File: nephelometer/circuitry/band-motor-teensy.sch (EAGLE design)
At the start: 20 parts, among them IC3 7805TV, J1 2.1MMJACKTHM, U1 MotA, U2 MotA

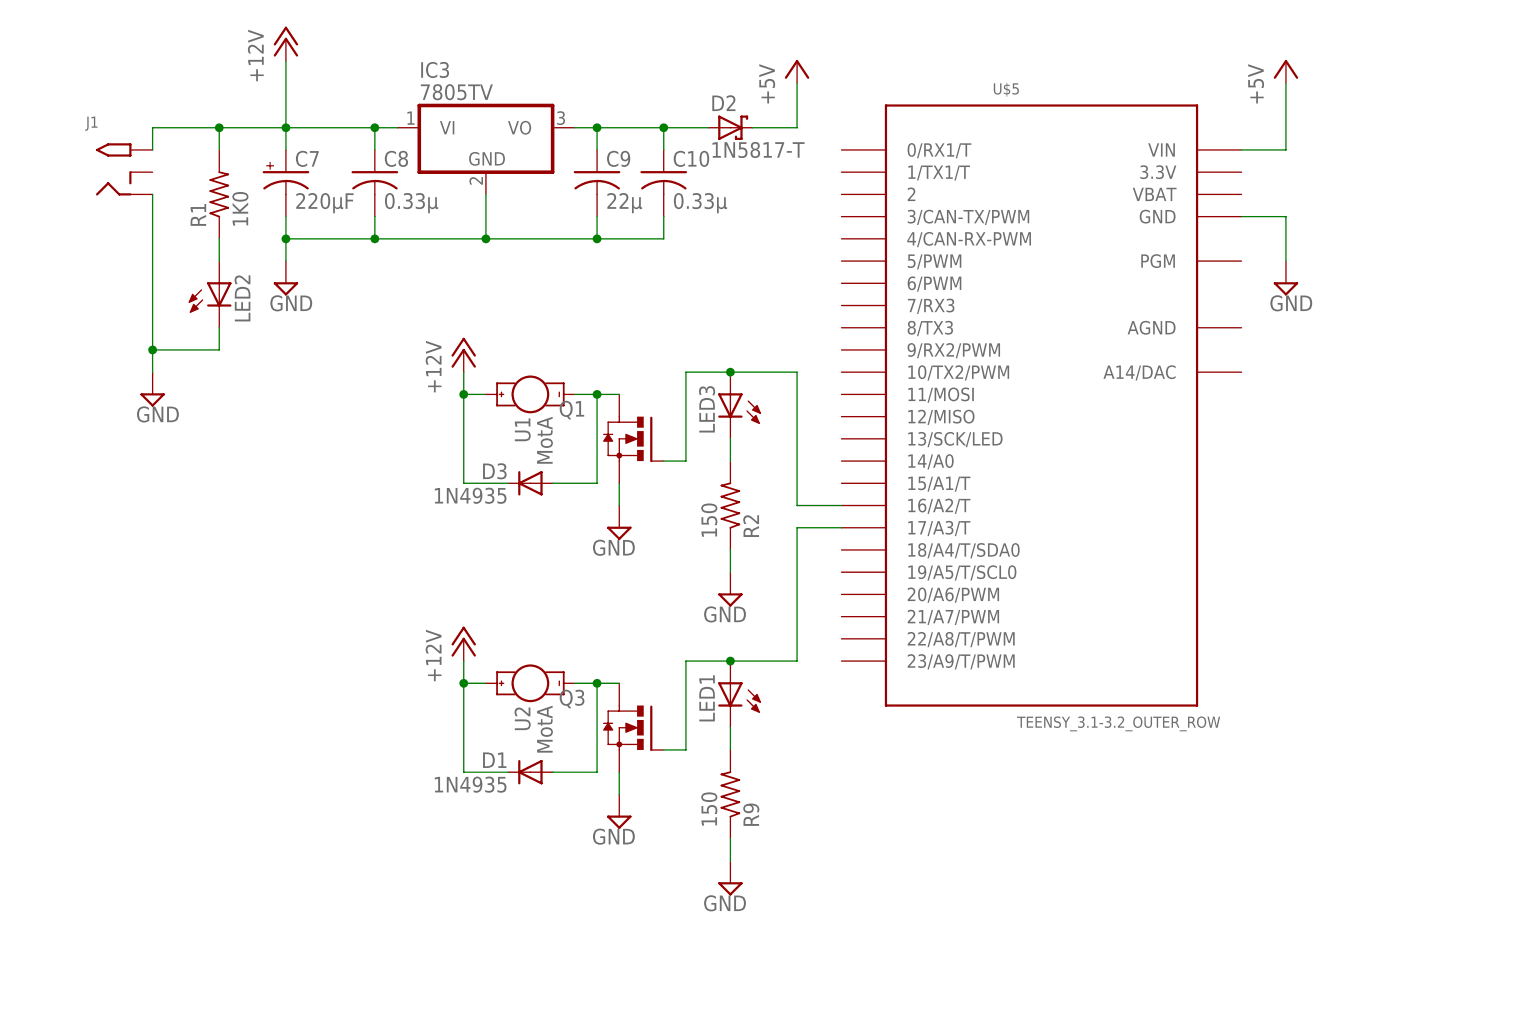
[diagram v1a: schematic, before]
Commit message: Designed motor power board to stack on nephelometer or run over RJ11 cable
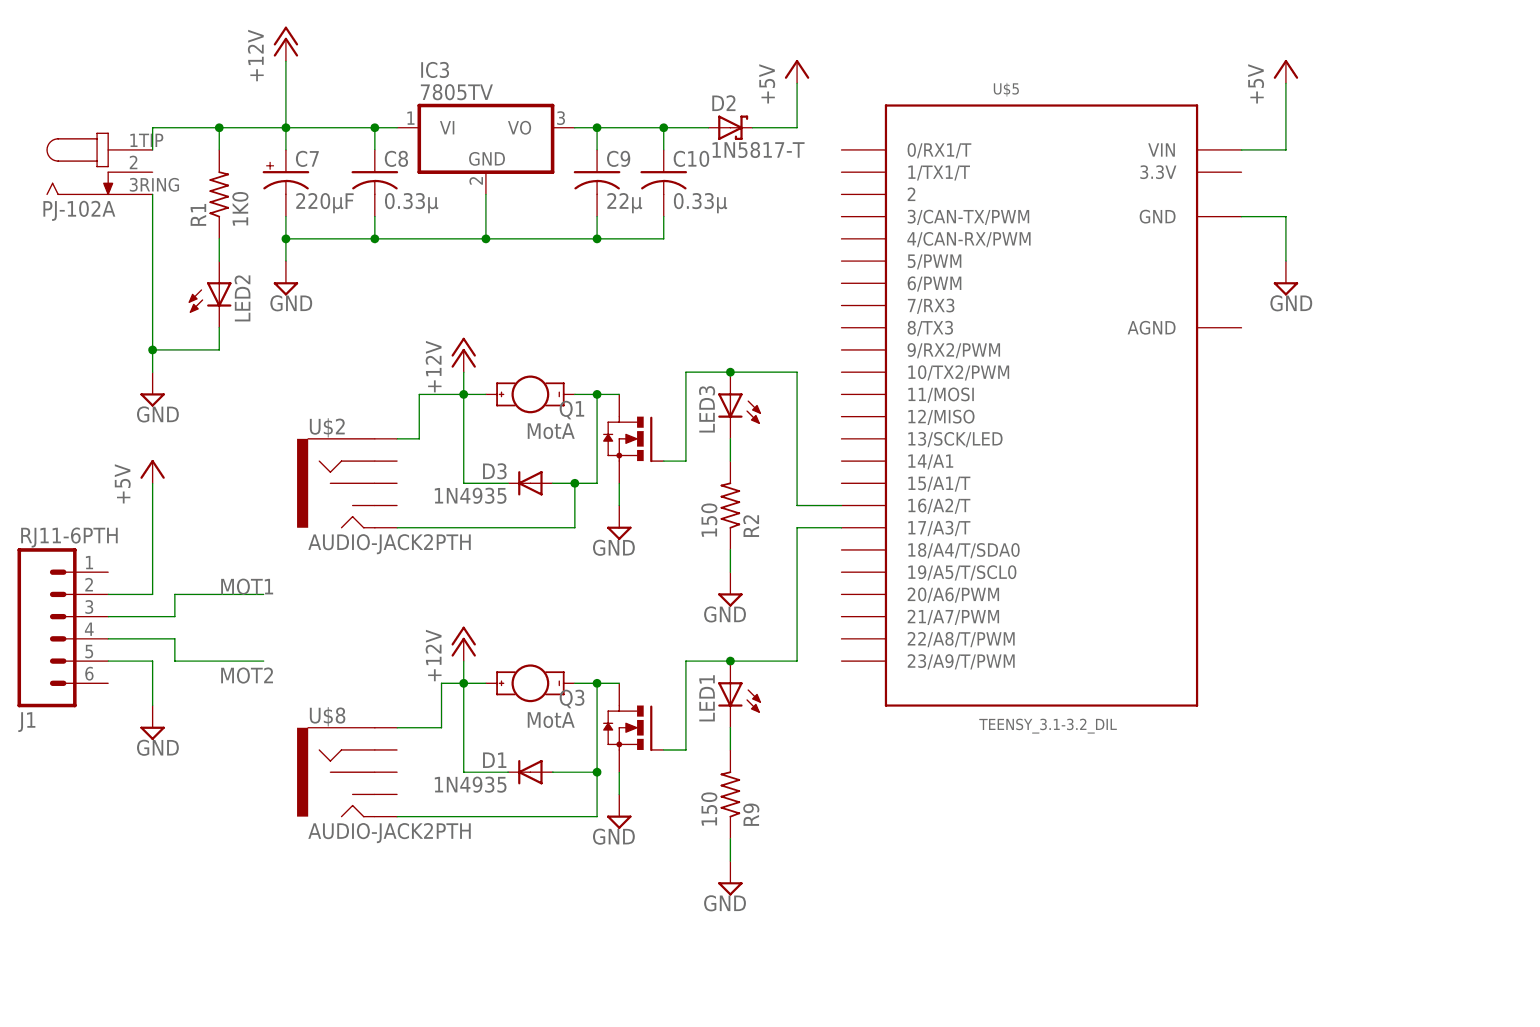
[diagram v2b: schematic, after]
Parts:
- added U$1: PJ-102A, ingolia:PJ-102A
- added U$2, U$8: AUDIO-JACK2PTH, SparkFun-Connectors:AUDIO-JACK2PTH
- J1: value 2.1MMJACKTHM -> RJ11-6PTH; device adafruit:2.1MMJACKTHM -> SparkFun-Connectors:RJ11-6PTH; DIGIKEY# CP-102A-ND -> (none); DIGIKEY2# 102-3623-ND -> (none); MANF CUI Inc -> (none); MANF# PJ-102A -> (none); MANF2 CUI Inc -> (none); MANF2# SWI24-12-N-P5 -> (none)
- R2, R9: device adafruit:R-US_0204/2V -> adafruit:R-US_0207/10
- U$5: value TEENSY_3.1-3.2_OUTER_ROW -> TEENSY_3.1-3.2_DIL; device Teensy_3_and_LC_Series_Boards_v1.4:TEENSY_3.1-3.2_OUTER_ROW -> Teensy_3_and_LC_Series_Boards_v1.4:TEENSY_3.1-3.2_DIL
- U1, U2: device ingolia:1X02_MOTOR -> ingolia:1X02_3.5MM_MOT
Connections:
- removed net N$19: LED1.A, Q3.G, U$5.17/A3/T
- removed net N$6: LED3.A, Q1.G, U$5.16/A2/T
- new net MOT1: J1.3, LED3.A, Q1.G, U$5.16/A2/T
- new net MOT2: J1.4, LED1.A, Q3.G, U$5.17/A3/T
- net +12V: now also U$1.3TIP, U$2.SLEEVE, U$8.SLEEVE; no longer J1.TIP
- net +5V: now also J1.2
- net GND: now also J1.5, U$1.1RING; no longer J1.RING
- net N$3: now also U$8.TIP
- net N$4: now also U$2.TIP

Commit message: Motor control with transistor gating MOSFET, shutoff when disconnected
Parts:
- removed U$1: PJ-102A, ingolia:PJ-102A
- removed U$5: TEENSY_3.1-3.2_DIL, Teensy_3_and_LC_Series_Boards_v1.4:TEENSY_3.1-3.2_DIL
- added J4: RJ11-6PTH, SparkFun-Connectors:RJ11-6PTH
- added MCU1: TEENSY_3.1-3.2_DIL, Teensy_3_and_LC_Series_Boards_v1.4:TEENSY_3.1-3.2_DIL
- added R10, R3, R5, R7: 1K0, adafruit:R-US_0207/10
- added R11, R6: 150R, adafruit:R-US_0207/10
- added R4, R8: 4K7, adafruit:R-US_0207/10
- added T1, T2: 2N2222, adafruit:2N2222
- D1: value 1N4935 -> 1N5817-T; device adafruit:1N4004 -> diode:1N5817-T; DIGIKEY# 1N4935FSCT-ND -> 1N5817FSCT-ND; MANF# 1N4935 -> 1N5817
- D2: value 1N5817-T -> 1N4935; device diode:1N5817-T -> adafruit:1N4004; DIGIKEY# 1N5817FSCT-ND -> 1N4935FSCT-ND; MANF# 1N5817 -> 1N4935
- J1: value RJ11-6PTH -> PJ-102A; device SparkFun-Connectors:RJ11-6PTH -> ingolia:PJ-102A
- LED1: device adafruit:LED3MM -> adafruit:LED5MM; DIGIKEY# 754-1275-ND -> 754-1735-ND; MANF# WP7113SRD/D -> WP7113SGD
- LED2: device adafruit:LED5MM -> adafruit:LED3MM; DIGIKEY# 754-1735-ND -> 754-1275-ND; MANF# WP7113SGD -> WP7113SRD/D
- R2, R9: value 150 -> 1K0
- renumbered C10 to C4, C7 to C1, C8 to C2, C9 to C3, IC3 to IC1, Q3 to Q2, U$2 to J3, U$8 to J6, U1 to J2, U2 to J5
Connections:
- new net N$6: R2.1, R3.1, T1.B
- new net N$7: R7.1, R9.1, T2.B
- new net N$8: Q1.G, R4.1, T1.C
- new net N$9: Q2.G, R8.1, T2.C
- net +12V: now also D2.C, J1.3TIP; no longer D1.C, U$1.3TIP
- net +5V: now also D1.C, J4.2, MCU1.VIN, R2.2, R4.2, R7.2, R8.2; no longer D2.C, J1.2, U$5.VIN
- net GND: now also J1.1RING, J4.5, LED1.C, MCU1.GND, R10.1, R11.1, R3.2, R5.1, R6.1, R9.2; no longer J1.5, LED2.C, R2.1, R9.1, U$1.1RING, U$5.GND
- net MOT1: now also J4.3, LED2.A, MCU1.16/A2/T, R5.2, T1.E; no longer J1.3, LED3.A, Q1.G, U$5.16/A2/T
- net MOT2: now also J4.4, LED3.A, MCU1.17/A3/T, R10.2, T2.E; no longer J1.4, LED1.A, Q2.G, U$5.17/A3/T
- net N$1: now also LED1.A; no longer LED2.A
- net N$16: now also LED3.C, R11.2; no longer LED1.C, R9.2
- net N$2: now also D1.A; no longer D2.A
- net N$3: now also D3.A; no longer D1.A
- net N$4: now also D2.A; no longer D3.A
- net N$5: now also LED2.C, R6.2; no longer LED3.C, R2.2
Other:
- moved on the sheet: D3, LED1, LED2, LED3, R2, R9

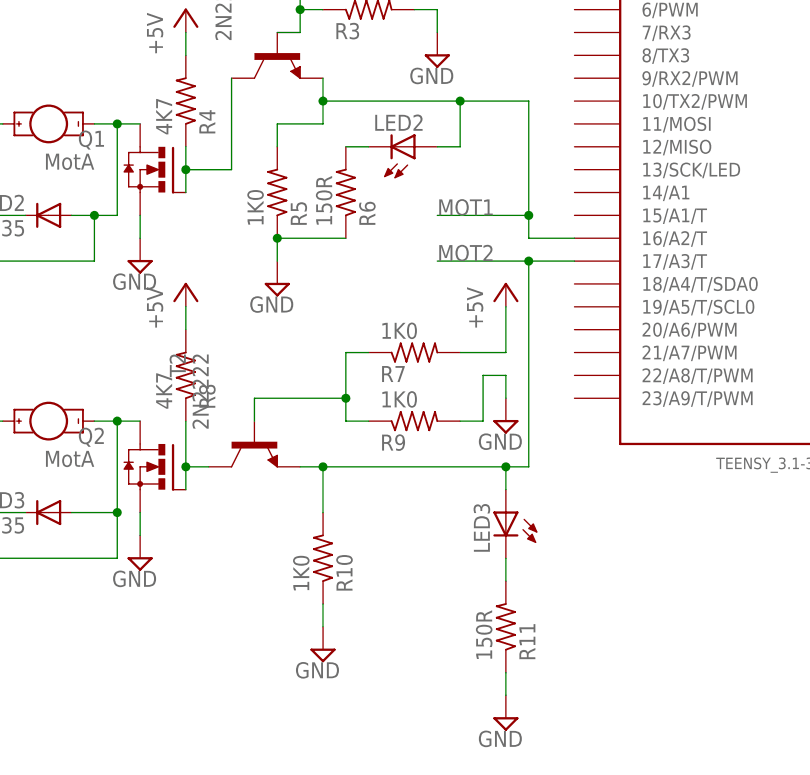
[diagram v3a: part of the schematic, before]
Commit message: Revised detector board circuit, picked filter values, finalized parts
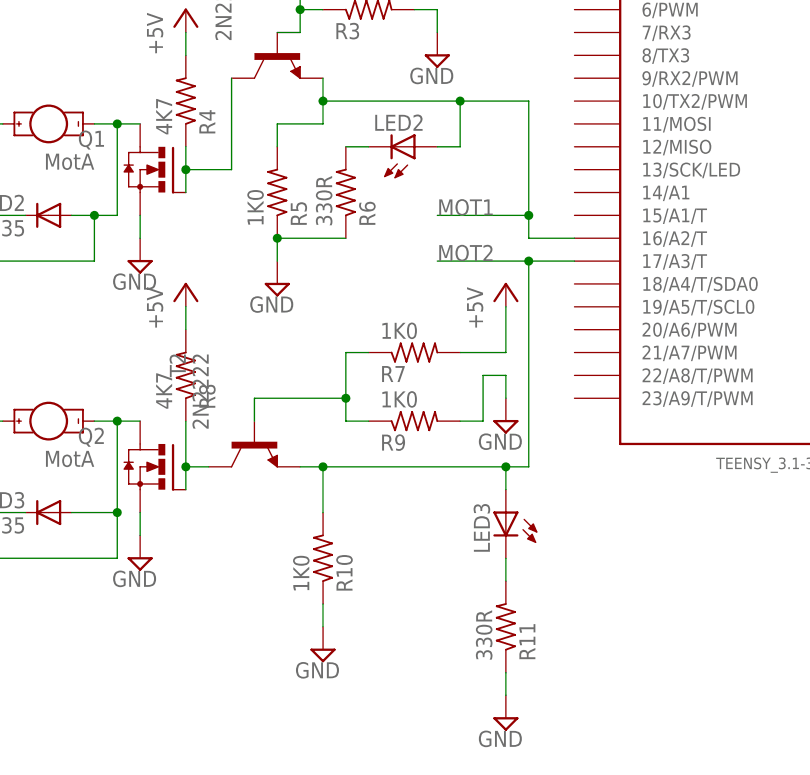
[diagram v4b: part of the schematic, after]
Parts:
- J1: DIGIKEY# (none) -> CP-102A-ND; MANF (none) -> CUI Inc.; MANF# (none) -> PJ-102A
- J2, J5: DIGIKEY# SC1455-ND -> ED2740-ND; MANF Switchcraft Inc. -> On Shore Technology Inc.; MANF# 35PM1 -> OSTTE020104
- J3, J6: DIGIKEY# (none) -> CP1-3523N-ND; MANF (none) -> CUI Inc.; MANF# (none) -> SJ1-3523N
- J4: DIGIKEY# (none) -> AE10383-ND; MANF (none) -> Assmann WSW Components; MANF# (none) -> -2004-1-4-LP-N-R
- MCU1: DIGIKEY# (none) -> SAM1198-14-ND; DIGIKEY2# (none) -> SAM1198-14-ND; MANF (none) -> Samtec Inc.; MANF# (none) -> SSQ-114-03-G-S; MANF2 (none) -> Samtec Inc.; MANF2# (none) -> SSQ-114-03-G-S
- Q1, Q2: DIGIKEY# IRLU120NPBF-ND -> IRLB8721PBF-ND; MANF# IRLU120NPBF -> IRLB8721PBF
- R10, R2, R3, R5, R7, R9: DIGIKEY# CF14JT150RCT-ND -> S1KHCT-ND; MANF# CF14JT150R -> CFM12JT1K00
- R11, R6: value 150R -> 330R; DIGIKEY# CF14JT150RCT-ND -> CF14JT330RCT-ND; MANF# CF14JT150R -> CF14JT330R
- R4, R8: DIGIKEY# CF14JT150RCT-ND -> CF14JT4K70CT-ND; MANF# CF14JT150R -> CF14JT4K70
- T1, T2: DIGIKEY# (none) -> PN2222ATFCT-ND; MANF (none) -> Fairchild Semiconductor; MANF# (none) -> PN2222ATF
